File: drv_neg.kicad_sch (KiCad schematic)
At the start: 29 parts, among them U4 74HCT595, U5 74HCT595, U6 74HCT595, U7 ULN2803A, U8 ULN2803A, U9 ULN2803A

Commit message: moar woerk
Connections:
- net GND: no longer U9.4 (I4), U9.5 (I5), U9.6 (I6), U9.7 (I7), U9.8 (I8)
- net ROW_N0: now also U7.11 (O8); no longer U7.18 (O1)
- net ROW_N1: now also U7.12 (O7); no longer U7.17 (O2)
- net ROW_N10: now also U8.13 (O6); no longer U8.16 (O3)
- net ROW_N11: now also U8.14 (O5); no longer U8.15 (O4)
- net ROW_N12: now also U8.15 (O4); no longer U8.14 (O5)
- net ROW_N13: now also U8.16 (O3); no longer U8.13 (O6)
- net ROW_N14: now also U8.17 (O2); no longer U8.12 (O7)
- net ROW_N15: now also U8.18 (O1); no longer U8.11 (O8)
- net ROW_N16: now also U9.11 (O8); no longer U9.18 (O1)
- net ROW_N17: now also U9.12 (O7); no longer U9.17 (O2)
- net ROW_N18: now also U9.13 (O6); no longer U9.16 (O3)
- net ROW_N2: now also U7.13 (O6); no longer U7.16 (O3)
- net ROW_N3: now also U7.14 (O5); no longer U7.15 (O4)
- net ROW_N4: now also U7.15 (O4); no longer U7.14 (O5)
- net ROW_N5: now also U7.16 (O3); no longer U7.13 (O6)
- net ROW_N6: now also U7.17 (O2); no longer U7.12 (O7)
- net ROW_N7: now also U7.18 (O1); no longer U7.11 (O8)
- net ROW_N8: now also U8.11 (O8); no longer U8.18 (O1)
- net ROW_N9: now also U8.12 (O7); no longer U8.17 (O2)
- net ROW_N_G0: now also R77.1, U7.8 (I8); no longer R60.1, U7.1 (I1)
- net ROW_N_G1: now also R75.1, U7.7 (I7); no longer R63.1, U7.2 (I2)
- net ROW_N_G10: now also R74.1, U8.6 (I6); no longer R67.1, U8.3 (I3)
- net ROW_N_G11: now also R72.1, U8.5 (I5); no longer R70.1, U8.4 (I4)
- net ROW_N_G12: now also R70.1, U8.4 (I4); no longer R72.1, U8.5 (I5)
- net ROW_N_G13: now also R67.1, U8.3 (I3); no longer R74.1, U8.6 (I6)
- net ROW_N_G14: now also R64.1, U8.2 (I2); no longer R76.1, U8.7 (I7)
- net ROW_N_G15: now also R61.1, U8.1 (I1); no longer R78.1, U8.8 (I8)
- net ROW_N_G16: now also R68.1, U9.8 (I8); no longer R62.1, U9.1 (I1)
- net ROW_N_G17: now also U9.7 (I7); no longer U9.2 (I2)
- net ROW_N_G18: now also R62.1, U9.6 (I6); no longer R68.1, U9.3 (I3)
- net ROW_N_G2: now also R73.1, U7.6 (I6); no longer R66.1, U7.3 (I3)
- net ROW_N_G3: now also R71.1, U7.5 (I5); no longer R69.1, U7.4 (I4)
- net ROW_N_G4: now also R69.1, U7.4 (I4); no longer R71.1, U7.5 (I5)
- net ROW_N_G5: now also R66.1, U7.3 (I3); no longer R73.1, U7.6 (I6)
- net ROW_N_G6: now also R63.1, U7.2 (I2); no longer R75.1, U7.7 (I7)
- net ROW_N_G7: now also R60.1, U7.1 (I1); no longer R77.1, U7.8 (I8)
- net ROW_N_G8: now also R78.1, U8.8 (I8); no longer R61.1, U8.1 (I1)
- net ROW_N_G9: now also R76.1, U8.7 (I7); no longer R64.1, U8.2 (I2)
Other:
- moved on the sheet: R62, R65, R68

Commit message: more work
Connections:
- net ROW_N_DO: now reaches U6.9 (QH')
- no-connect marks 11 -> 10
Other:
- moved on the sheet: C4, C5, C6, R59, U4, U5, U6

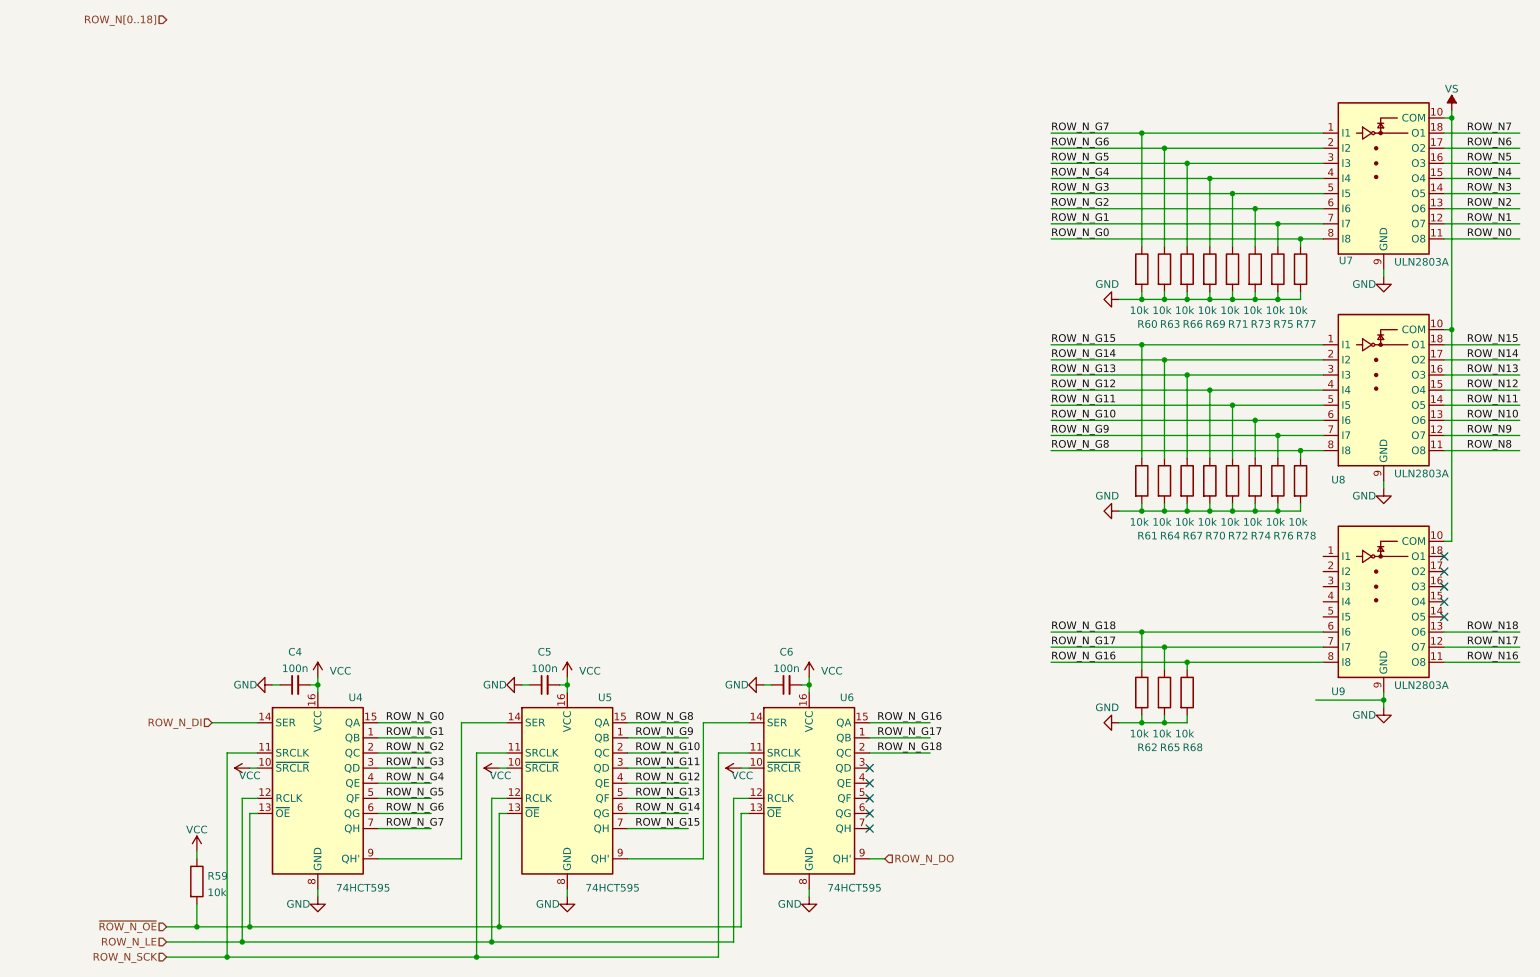
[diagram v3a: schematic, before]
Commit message: Change negative drivers to a TLE75008-ESD, octal low side driver.
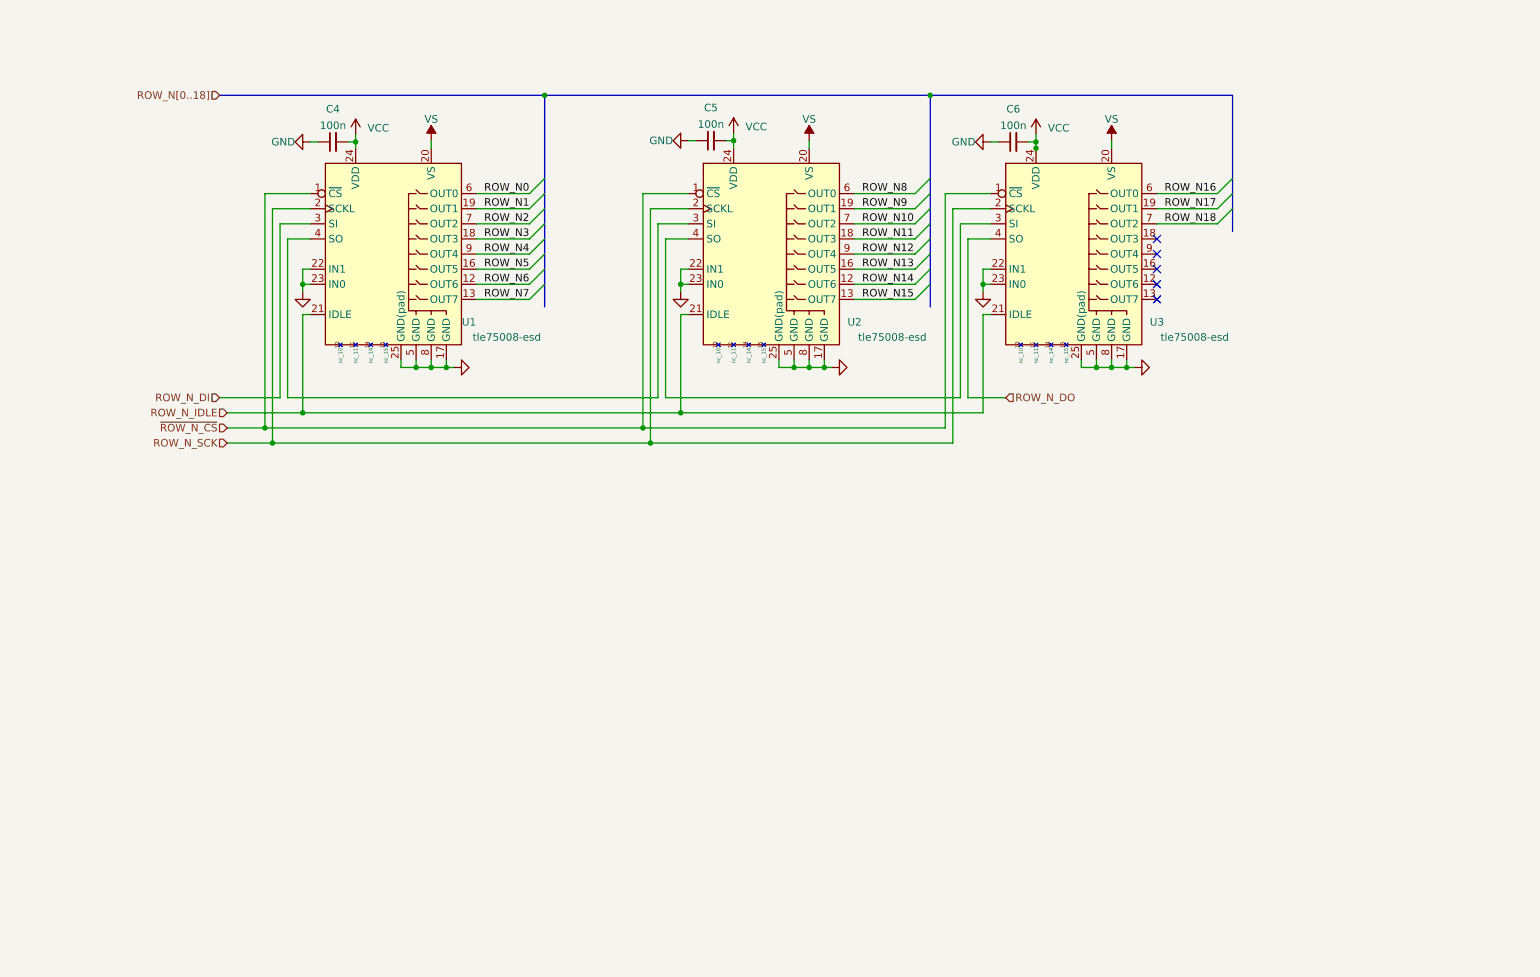
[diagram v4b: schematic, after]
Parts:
- removed R59, R60, R61, R62, R63, R64, R65, R66, R67, R68, R69, R70, R71, R72, R73, R74, R75, R76, R77, R78: 10k, Resistor_SMD:R_0603_1608Metric, symbol Device:R
- removed U4, U5, U6: 74HCT595, Package_SO:SOIC-16_3.9x9.9mm_P1.27mm, symbol 74xx:74HCT595
- removed U7, U8, U9: ULN2803A, Package_SO:SOIC-18W_7.5x11.6mm_P1.27mm, symbol Transistor_Array:ULN2803A
- added U1, U2, U3: tle75008-esd, vogelchr_package_so:Infineon-PG-TSDSO-24-51, symbol vogelchr_ic:tle75008-esd
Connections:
- net GND: now also U1.17 (GND), U1.22 (IN1), U1.23 (IN0), U1.25 (GND(pad)), U1.5 (GND), U1.8 (GND), U2.17 (GND), U2.22 (IN1), U2.23 (IN0), U2.25 (GND(pad)), U2.5 (GND), U2.8 (GND), U3.17 (GND), U3.22 (IN1), U3.23 (IN0), U3.25 (GND(pad)), U3.5 (GND), U3.8 (GND)
- net ROW_N0: now also U1.6 (OUT0)
- net ROW_N1: now also U1.19 (OUT1)
- net ROW_N10: now also U2.7 (OUT2)
- net ROW_N11: now also U2.18 (OUT3)
- net ROW_N12: now also U2.9 (OUT4)
- net ROW_N13: now also U2.16 (OUT5)
- net ROW_N14: now also U2.12 (OUT6)
- net ROW_N15: now also U2.13 (OUT7)
- net ROW_N16: now also U3.6 (OUT0)
- net ROW_N17: now also U3.19 (OUT1)
- net ROW_N18: now also U3.7 (OUT2)
- net ROW_N2: now also U1.7 (OUT2)
- net ROW_N3: now also U1.18 (OUT3)
- net ROW_N4: now also U1.9 (OUT4)
- net ROW_N5: now also U1.16 (OUT5)
- net ROW_N6: now also U1.12 (OUT6)
- net ROW_N7: now also U1.13 (OUT7)
- net ROW_N8: now also U2.6 (OUT0)
- net ROW_N9: now also U2.19 (OUT1)
- net ROW_N_DI: now also U1.3 (SI)
- net ROW_N_DO: now also U3.4 (SO)
- net ROW_N_SCK: now also U1.2 (SCKL), U2.2 (SCKL), U3.2 (SCKL)
- net VCC: now also U1.24 (VDD), U2.24 (VDD), U3.24 (VDD)
- net VS: now also U1.20 (VS), U2.20 (VS), U3.20 (VS)
- new net: U1.4 (SO), U2.3 (SI)
- new net: U2.4 (SO), U3.3 (SI)
- new net ROW_N_IDLE: U1.21 (IDLE), U2.21 (IDLE), U3.21 (IDLE)
- new net ~{ROW_N_CS}: U1.1 (~{CS}), U2.1 (~{CS}), U3.1 (~{CS})
- no-connect marks 10 -> 5
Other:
- moved on the sheet: C4, C5, C6
